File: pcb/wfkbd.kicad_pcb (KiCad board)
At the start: 2 copper layers, 132 x 98.5 mm, 96 parts, among them SW1 KEY, SW10 KEY, SW11 KEY, SW12 KEY, SW13 KEY, SW14 KEY, SW15 KEY, SW16 KEY, SW17 KEY, SW18 KEY, SW19 KEY, SW2 KEY, SW20 KEY, SW21 KEY, SW22 KEY, SW23 KEY, SW24 KEY, SW25 KEY, SW26 KEY, SW27 KEY, SW28 KEY, SW29 KEY, SW3 KEY, SW30 KEY, SW31 KEY, SW32 KEY, SW33 KEY, SW34 KEY, SW35 KEY, SW4 KEY, SW5 KEY, SW6 KEY, SW7 KEY, SW8 KEY, SW9 KEY, U1 ProMicro

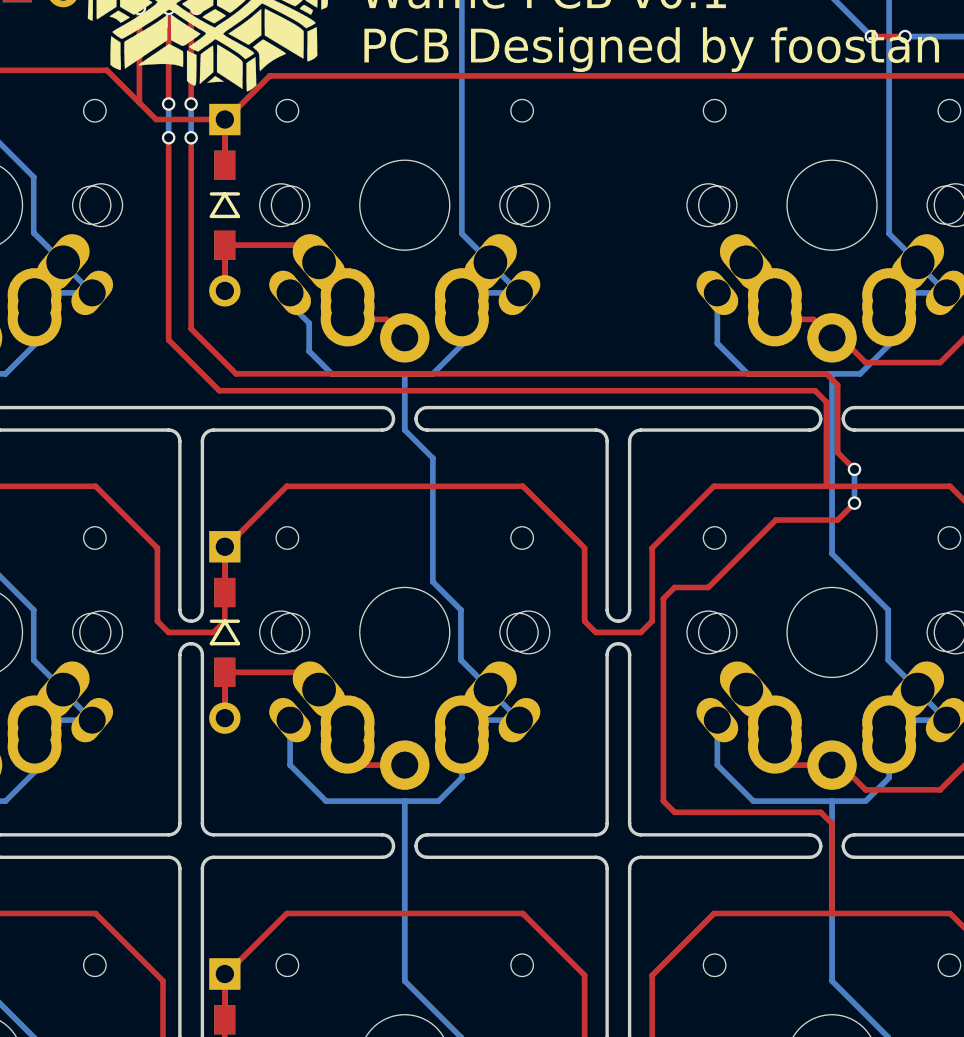
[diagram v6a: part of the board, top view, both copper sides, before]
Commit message: Add holes
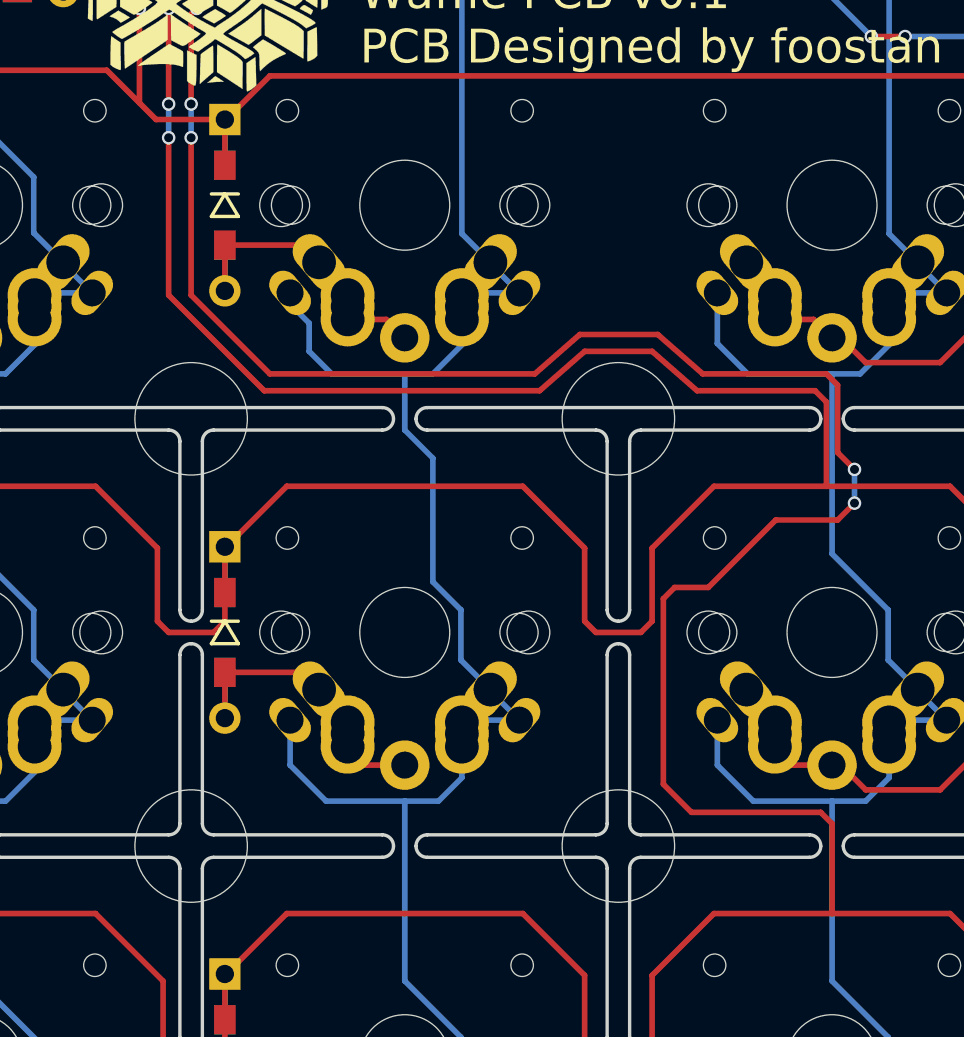
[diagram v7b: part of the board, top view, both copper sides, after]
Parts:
- added ?: , kbd:LegoHole, F.Cu at (116.5, 97.5)
- added ?: , kbd:LegoHole, F.Cu at (97.5, 97.5)
- added ?: , kbd:LegoHole, F.Cu at (116.5, 116.5)
- added ?: , kbd:LegoHole, F.Cu at (97.5, 116.5)
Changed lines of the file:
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@@
     (links 578)
     (no_connects 3)
-    (area 40.924999 36.424999 173.075001 135.075001)
+    (area 39.275 35.149999 174.2625 135.275001)
     (thickness 1.6)
     (drawings 338)
-    (tracks 1335)
+    (tracks 1343)
     (zones 0)
-    (modules 96)
+    (modules 100)
     (nets 59)
   )
@@
     (visible_elements FFFFFF7F)
     (pcbplotparams
-      (layerselection 0x00030_80000001)
+      (layerselection 0x01c30_80000001)
       (usegerberextensions false)
       (excludeedgelayer true)
@@
       (padsonsilk false)
       (subtractmaskfromsilk false)
-      (outputformat 1)
+      (outputformat 3)
       (mirror false)
-      (drillshape 1)
+      (drillshape 0)
       (scaleselection 1)
-      (outputdirectory ""))
+      (outputdirectory ../case/))
   )
   (net 0 "")
@@
     (add_net sda)
   )
+  (module kbd:LegoHole (layer F.Cu)
+    (at 116.5 97.5)
+    (descr "Mounting Hole 5mm")
+    (tags "mounting hole 5mm")
+    (attr virtual)
+    (fp_text reference "" (at 0 -4) (layer F.Fab)
+      (effects (font (size 1 1) (thickness 0.15)))
+    )
+    (fp_text value "" (at 0 4) (layer F.Fab)
+      (effects (font (size 1 1) (thickness 0.15)))
+    )
+    (fp_text user %R (at 0.3 0) (layer F.Fab)
+      (effects (font (size 1 1) (thickness 0.15)))
+    )
+    (pad "" np_thru_hole circle (at 0 0) (size 5 5) (drill 5) (layers *.Cu *.Mask))
+  )
+  (module kbd:LegoHole (layer F.Cu)
+    (at 97.5 97.5)
+    (descr "Mounting Hole 5mm")
+    (tags "mounting hole 5mm")
+    (attr virtual)
+    (fp_text reference "" (at 0 -4) (layer F.Fab)
+      (effects (font (size 1 1) (thickness 0.15)))
+    )
+    (fp_text value "" (at 0 4) (layer F.Fab)
+      (effects (font (size 1 1) (thickness 0.15)))
+    )
+    (fp_text user %R (at 0.3 0) (layer F.Fab)
+      (effects (font (size 1 1) (thickness 0.15)))
+    )
+    (pad "" np_thru_hole circle (at 0 0) (size 5 5) (drill 5) (layers *.Cu *.Mask))
+  )
+  (module kbd:LegoHole (layer F.Cu)
+    (at 116.5 116.5)
+    (descr "Mounting Hole 5mm")
+    (tags "mounting hole 5mm")
+    (attr virtual)
+    (fp_text reference "" (at 0 -4) (layer F.Fab)
+      (effects (font (size 1 1) (thickness 0.15)))
+    )
+    (fp_text value "" (at 0 4) (layer F.Fab)
+      (effects (font (size 1 1) (thickness 0.15)))
+    )
+    (fp_text user %R (at 0.3 0) (layer F.Fab)
+      (effects (font (size 1 1) (thickness 0.15)))
+    )
+    (pad "" np_thru_hole circle (at 0 0) (size 5 5) (drill 5) (layers *.Cu *.Mask))
+  )
+  (module kbd:LegoHole (layer F.Cu)
+    (at 97.5 116.5)
+    (descr "Mounting Hole 5mm")
+    (tags "mounting hole 5mm")
+    (attr virtual)
+    (fp_text reference "" (at 0 -4) (layer F.Fab)
+      (effects (font (size 1 1) (thickness 0.15)))
+    )
+    (fp_text value "" (at 0 4) (layer F.Fab)
+      (effects (font (size 1 1) (thickness 0.15)))
+    )
+    (fp_text user %R (at 0.3 0) (layer F.Fab)
+      (effects (font (size 1 1) (thickness 0.15)))
+    )
+    (pad "" np_thru_hole circle (at 0 0) (size 5 5) (drill 5) (layers *.Cu *.Mask))
+  )
   (module kbd:D3_TH_SMD (layer F.Cu)
     (at 42 50 270)
@@
   (segment (start 96.5 65) (end 96.5 77.75) (width 0.25) (layer F.Cu) (net 32))
   (segment (start 99.31 62.19) (end 96.5 65) (width 0.25) (layer F.Cu) (net 32) (status 10))
-  (segment (start 96.5 94) (end 98.75 96.25) (width 0.25) (layer F.Cu) (net 32))
-  (segment (start 98.75 96.25) (end 125.25 96.25) (width 0.25) (layer F.Cu) (net 32))
-  (segment (start 96.5 85) (end 96.5 94) (width 0.25) (layer F.Cu) (net 32))
+  (segment (start 96.5 92) (end 100.75 96.25) (width 0.25) (layer F.Cu) (net 32))
+  (segment (start 100.75 96.25) (end 113 96.25) (width 0.25) (layer F.Cu) (net 32))
+  (segment (start 113 96.25) (end 115 94.5) (width 0.25) (layer F.Cu) (net 32))
+  (segment (start 115 94.5) (end 118 94.5) (width 0.25) (layer F.Cu) (net 32))
+  (segment (start 118 94.5) (end 120 96.25) (width 0.25) (layer F.Cu) (net 32))
+  (segment (start 120 96.25) (end 125.25 96.25) (width 0.25) (layer F.Cu) (net 32))
+  (segment (start 96.5 85) (end 96.5 92) (width 0.25) (layer F.Cu) (net 32))
   (segment (start 125.75 96.75) (end 125.75 100.5) (width 0.25) (layer F.Cu) (net 32))
   (segment (start 137 103.19) (end 137 105.225) (width 0.25) (layer F.Cu) (net 32))
@@
   (via (at 127 101.25) (size 0.6) (drill 0.4) (layers F.Cu B.Cu) (net 40))
   (segment (start 99.27 64.73) (end 97.75 66.25) (width 0.25) (layer F.Cu) (net 40))
-  (segment (start 99.5 95.5) (end 125.75 95.5) (width 0.25) (layer F.Cu) (net 40))
-  (segment (start 97.5 93.5) (end 99.5 95.5) (width 0.25) (layer F.Cu) (net 40))
-  (segment (start 97.5 85) (end 97.5 93.5) (width 0.25) (layer F.Cu) (net 40))
+  (segment (start 101 95.5) (end 112.785714 95.5) (width 0.25) (layer F.Cu) (net 40))
+  (segment (start 112.785714 95.5) (end 114.785714 93.75) (width 0.25) (layer F.Cu) (net 40))
+  (segment (start 114.785714 93.75) (end 118.25 93.75) (width 0.25) (layer F.Cu) (net 40))
+  (segment (start 118.25 93.75) (end 120.25 95.5) (width 0.25) (layer F.Cu) (net 40))
+  (segment (start 120.25 95.5) (end 125.75 95.5) (width 0.25) (layer F.Cu) (net 40))
+  (segment (start 97.5 92) (end 101 95.5) (width 0.25) (layer F.Cu) (net 40))
+  (segment (start 97.5 85) (end 97.5 92) (width 0.25) (layer F.Cu) (net 40))
   (via (at 97.5 85) (size 0.6) (drill 0.4) (layers F.Cu B.Cu) (net 40))
   (segment (start 97.5 83.5) (end 97.5 85) (width 0.25) (layer B.Cu) (net 40))
@@
   (segment (start 126 119.5) (end 126 115.5) (width 0.25) (layer F.Cu) (net 40))
   (segment (start 126 115.5) (end 125.5 115) (width 0.25) (layer F.Cu) (net 40))
-  (segment (start 125.5 115) (end 119 115) (width 0.25) (layer F.Cu) (net 40))
-  (segment (start 119 115) (end 118.5 114.5) (width 0.25) (layer F.Cu) (net 40))
-  (segment (start 118.5 114.5) (end 118.5 105.5) (width 0.25) (layer F.Cu) (net 40))
+  (segment (start 125.5 115) (end 119.75 115) (width 0.25) (layer F.Cu) (net 40))
+  (segment (start 119.75 115) (end 118.5 113.75) (width 0.25) (layer F.Cu) (net 40))
+  (segment (start 118.5 113.75) (end 118.5 105.5) (width 0.25) (layer F.Cu) (net 40))
   (segment (start 99.38 64.73) (end 99.27 64.73) (width 0.25) (layer F.Cu) (net 40))
   (segment (start 99 122.19) (end 99 124.225) (width 0.25) (layer B.Cu) (net 40))

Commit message: Update split lines
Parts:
- removed the ? at (116.5, 97.5)
- removed the ? at (59.5, 97.5)
- removed the ? at (59.5, 78.5)
- removed the ? at (135.5, 97.5)
- removed the ? at (97.5, 97.5)
- removed the ? at (116.5, 116.5)
- removed the ? at (97.5, 116.5)
- removed the ? at (59.5, 59.5)
- removed the ? at (59.5, 116.5)
- removed the ? at (78.5, 116.5)
- added ?: , kbd:LegoHole, F.Cu at (50.0, 59.5)
- added ?: , kbd:LegoHole, F.Cu at (97.5, 126.0)
- added ?: , kbd:LegoHole, F.Cu at (116.5, 107.0)
- added ?: , kbd:LegoHole, F.Cu at (116.5, 126.0)
- added ?: , kbd:LegoHole, F.Cu at (135.5, 126.0)
- added ?: , kbd:LegoHole, F.Cu at (135.5, 107.0)
- added ?: , kbd:LegoHole, F.Cu at (154.5, 107.0)
- added ?: , kbd:LegoHole, F.Cu at (154.5, 126.0)
- added ?: , kbd:LegoHole, F.Cu at (50.0, 78.5)
- added ?: , kbd:LegoHole, F.Cu at (50.0, 97.5)
- added ?: , kbd:LegoHole, F.Cu at (50.0, 116.6)
- added ?: , kbd:LegoHole, F.Cu at (59.5, 107.0)
- added ?: , kbd:LegoHole, F.Cu at (59.5, 126.0)
- added ?: , kbd:LegoHole, F.Cu at (78.5, 126.0)
- added ?: , kbd:LegoHole, F.Cu at (78.5, 107.0)
- added ?: , kbd:LegoHole, F.Cu at (97.5, 107.0)
- U1: footprint kbd:ProMicro -> Keebio-Parts:ArduinoProMicro
- moved D23 11.3 mm to (69.0, 115.0), turned to 180 degrees
- moved D24 11.3 mm to (88.0, 115.0), turned to 180 degrees
- moved D25 11.3 mm to (107.0, 115.0), turned to 180 degrees
- moved D26 11.3 mm to (126.0, 115.0), turned to 180 degrees
- moved D27 11.3 mm to (145.0, 115.0), turned to 180 degrees
- moved D30 11.3 mm to (69.0, 134.0), turned to 180 degrees
- moved D31 11.3 mm to (88.0, 134.0), turned to 180 degrees
- moved D32 11.3 mm to (107.0, 134.0), turned to 180 degrees
- moved D33 11.3 mm to (126.0, 134.0), turned to 180 degrees
- moved D34 11.3 mm to (145.0, 134.0), turned to 180 degrees
- moved ? 9.50 mm to (164.0, 78.5)
- moved ? 9.50 mm to (164.0, 97.5)
- moved ? 9.50 mm to (164.0, 116.5)
- renumbered TRS to TRRS
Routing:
- net col0: track 296.9 -> 323.0 mm
- net col6: track 248.7 -> 274.7 mm
- net row2: track 210.4 -> 193.6 mm
- net row1: track 205.0 -> 188.5 mm
- net row0: track 205.3 -> 196.5 mm
- net row3: track 276.3 -> 283.2 mm
- net Net-(D30-Pad2): track 19.8 -> 13.5 mm
- net Net-(D23-Pad2): track 19.8 -> 13.5 mm
- net col5: track 183.4 -> 189.1 mm
- net Net-(D26-Pad2): track 19.8 -> 16.2 mm, vias 0 -> 1
- net Net-(D34-Pad2): track 13.8 -> 16.9 mm, vias 0 -> 1
- net Net-(D31-Pad2): track 13.8 -> 16.9 mm, vias 0 -> 1
- net Net-(D33-Pad2): track 19.5 -> 16.6 mm, vias 0 -> 1
- net Net-(D32-Pad2): track 13.8 -> 16.6 mm, vias 0 -> 1
- net Net-(D22-Pad2): track 12.5 -> 15.2 mm
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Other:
- outline, holes or cut-outs redrawn
- board text added: "RESET"
- board text added: "TRRS"
- board text added: "wfkbd v1.0 PCB Designed by foostan"
- board text removed: "Waffle PCB v0.1 PCB Designed by foostan"
